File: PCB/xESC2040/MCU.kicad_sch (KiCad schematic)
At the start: 20 parts, among them J6 Conn_01x02, U2 RP2040, U3 W25Q128JVP, Y1 Crystal

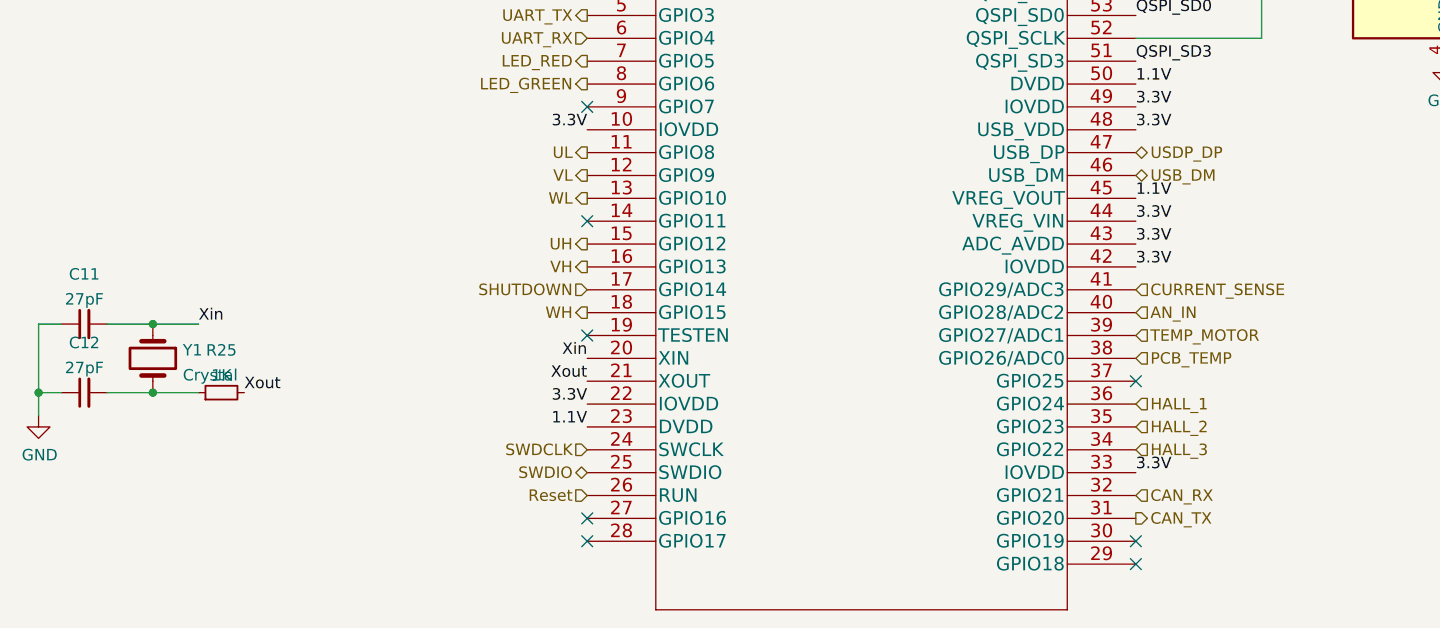
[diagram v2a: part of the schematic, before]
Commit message: added CAN, WIP
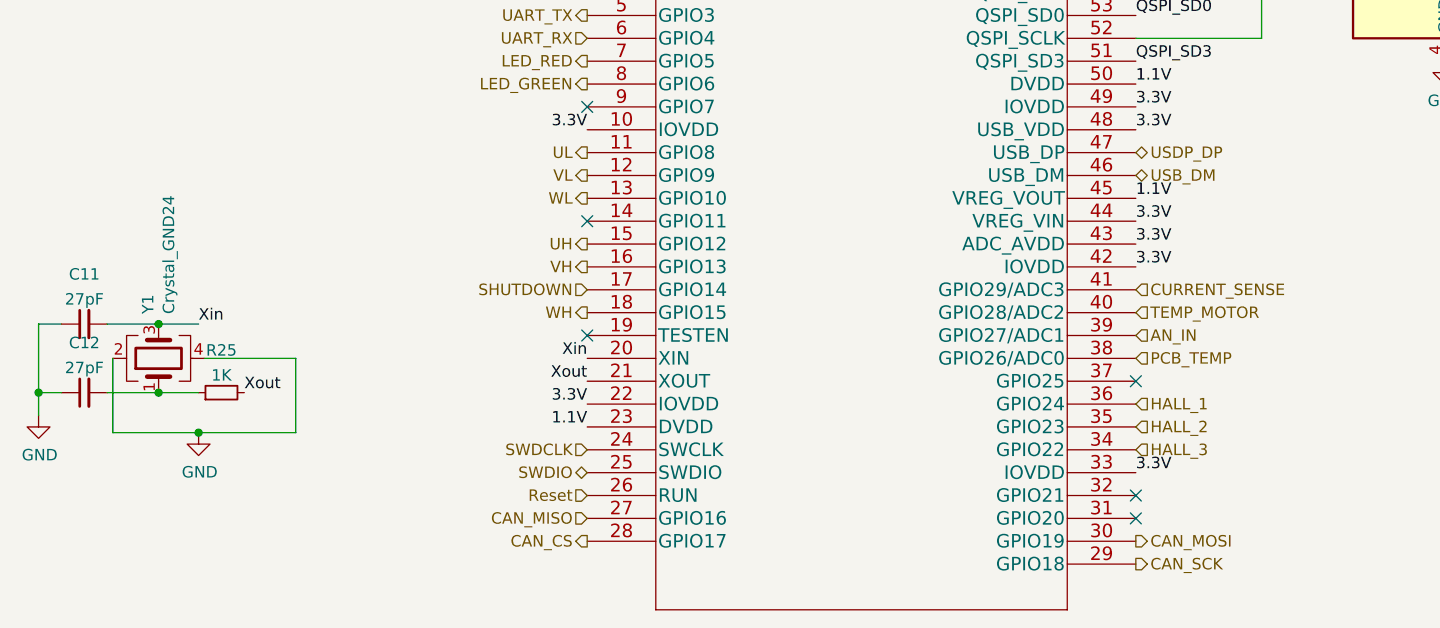
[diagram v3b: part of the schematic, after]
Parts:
- removed Y1: Crystal, Crystal:Crystal_SMD_3225-4Pin_3.2x2.5mm, symbol Device:Crystal
- added Y1: Crystal_GND24, Crystal:Crystal_SMD_3225-4Pin_3.2x2.5mm, symbol Device:Crystal_GND24
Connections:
- net AN_IN: now also U2.39 (GPIO27/ADC1); no longer U2.40 (GPIO28/ADC2)
- net GND: now also Y1.2, Y1.4
- net TEMP_MOTOR: now also U2.40 (GPIO28/ADC2); no longer U2.39 (GPIO27/ADC1)
- net Xin: now also Y1.3
- net CAN_MISO: now reaches U2.27 (GPIO16)
- net CAN_CS: now reaches U2.28 (GPIO17)
- net CAN_SCK: now reaches U2.29 (GPIO18)
- net CAN_MOSI: now reaches U2.30 (GPIO19)
- net at C12.2, R25.1: now also Y1.1
- net CAN_RX: no longer names the net of U2.32 (GPIO21)
- net CAN_TX: no longer names the net of U2.31 (GPIO20)
- no-connect marks 11 -> 9
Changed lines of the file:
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@@
   (junction (at 232.41 24.13) (diameter 0) (color 0 0 0 0)
   )
-  (junction (at 62.23 111.76) (diameter 0) (color 0 0 0 0)
+  (junction (at 67.31 123.825) (diameter 0) (color 0 0 0 0)
   )
   (junction (at 185.42 39.37) (diameter 0) (color 0 0 0 0)
@@
   (junction (at 177.8 21.59) (diameter 0) (color 0 0 0 0)
   )
+  (junction (at 62.865 111.76) (diameter 0) (color 0 0 0 0)
+  )
+  (junction (at 62.865 119.38) (diameter 0) (color 0 0 0 0)
+  )
   (junction (at 181.61 21.59) (diameter 0) (color 0 0 0 0)
   )
@@
   (junction (at 153.67 39.37) (diameter 0) (color 0 0 0 0)
   )
-  (junction (at 62.23 119.38) (diameter 0) (color 0 0 0 0)
-  )
   (junction (at 185.42 57.15) (diameter 0) (color 0 0 0 0)
   )
@@
   )
   (no_connect (at 110.49 100.33))
-  (no_connect (at 110.49 133.35))
   (no_connect (at 171.45 118.11))
   (no_connect (at 110.49 72.39))
   (no_connect (at 110.49 74.93))
+  (no_connect (at 171.45 130.81))
   (no_connect (at 110.49 69.85))
   (no_connect (at 110.49 87.63))
   (no_connect (at 110.49 113.03))
-  (no_connect (at 171.45 138.43))
-  (no_connect (at 171.45 135.89))
-  (no_connect (at 110.49 135.89))
+  (no_connect (at 171.45 133.35))
   (wire (pts (xy 185.42 74.93) (xy 185.42 80.01))
     (stroke (width 0) (type default) (color 0 0 0 0))
@@
     (stroke (width 0) (type default) (color 0 0 0 0))
   )
-  (wire (pts (xy 57.15 111.76) (xy 62.23 111.76))
+  (wire (pts (xy 57.15 111.76) (xy 62.865 111.76))
     (stroke (width 0) (type default) (color 0 0 0 0))
   )
@@
     (stroke (width 0) (type default) (color 0 0 0 0))
   )
+  (wire (pts (xy 62.865 119.38) (xy 67.31 119.38))
+    (stroke (width 0) (type default) (color 0 0 0 0))
+  )
   (wire (pts (xy 170.18 25.4) (xy 170.18 21.59))
     (stroke (width 0) (type default) (color 0 0 0 0))
@@
     (stroke (width 0) (type default) (color 0 0 0 0))
   )
+  (wire (pts (xy 67.945 115.57) (xy 78.105 115.57))
+    (stroke (width 0) (type default) (color 0 0 0 0))
+  )
   (wire (pts (xy 185.42 33.02) (xy 185.42 39.37))
     (stroke (width 0) (type default) (color 0 0 0 0))
@@
     (stroke (width 0) (type default) (color 0 0 0 0))
   )
+  (wire (pts (xy 78.105 115.57) (xy 78.105 123.825))
+    (stroke (width 0) (type default) (color 0 0 0 0))
+  )
   (wire (pts (xy 161.29 25.4) (xy 161.29 21.59))
     (stroke (width 0) (type default) (color 0 0 0 0))
   )
+  (wire (pts (xy 62.865 111.76) (xy 67.31 111.76))
+    (stroke (width 0) (type default) (color 0 0 0 0))
+  )
   (wire (pts (xy 146.05 21.59) (xy 153.67 21.59))
     (stroke (width 0) (type default) (color 0 0 0 0))
@@
     (stroke (width 0) (type default) (color 0 0 0 0))
   )
-  (wire (pts (xy 62.23 119.38) (xy 67.31 119.38))
+  (wire (pts (xy 78.105 123.825) (xy 67.31 123.825))
     (stroke (width 0) (type default) (color 0 0 0 0))
   )
@@
     (stroke (width 0) (type default) (color 0 0 0 0))
   )
-  (wire (pts (xy 62.23 111.76) (xy 67.31 111.76))
-    (stroke (width 0) (type default) (color 0 0 0 0))
-  )
   (wire (pts (xy 170.18 21.59) (xy 177.8 21.59))
     (stroke (width 0) (type default) (color 0 0 0 0))
@@
     (stroke (width 0) (type default) (color 0 0 0 0))
   )
-  (wire (pts (xy 57.15 119.38) (xy 62.23 119.38))
+  (wire (pts (xy 57.785 115.57) (xy 57.785 123.825))
+    (stroke (width 0) (type default) (color 0 0 0 0))
+  )
+  (wire (pts (xy 57.15 119.38) (xy 62.865 119.38))
     (stroke (width 0) (type default) (color 0 0 0 0))
   )
@@
   )
   (wire (pts (xy 52.07 111.76) (xy 49.53 111.76))
+    (stroke (width 0) (type default) (color 0 0 0 0))
+  )
+  (wire (pts (xy 67.31 123.825) (xy 57.785 123.825))
     (stroke (width 0) (type default) (color 0 0 0 0))
   )
@@
     (effects (font (size 1.27 1.27)) (justify left bottom))
   )
-  (hierarchical_label "CAN_TX" (shape output) (at 171.45 133.35 0)
-    (effects (font (size 1.27 1.27)) (justify left))
-  )
   (hierarchical_label "USDP_DP" (shape bidirectional) (at 171.45 92.71 0)
     (effects (font (size 1.27 1.27)) (justify left))
   )
+  (hierarchical_label "CAN_CS" (shape output) (at 110.49 135.89 180)
+    (effects (font (size 1.27 1.27)) (justify right))
+  )
   (hierarchical_label "UART_RX" (shape input) (at 110.49 80.01 180)
     (effects (font (size 1.27 1.27)) (justify right))
   )
-  (hierarchical_label "CAN_RX" (shape input) (at 171.45 130.81 0)
-    (effects (font (size 1.27 1.27)) (justify left))
-  )
-  (hierarchical_label "TEMP_MOTOR" (shape input) (at 171.45 113.03 0)
+  (hierarchical_label "TEMP_MOTOR" (shape input) (at 171.45 110.49 0)
     (effects (font (size 1.27 1.27)) (justify left))
   )
@@
     (effects (font (size 1.27 1.27)) (justify right))
   )
+  (hierarchical_label "CAN_MISO" (shape input) (at 110.49 133.35 180)
+    (effects (font (size 1.27 1.27)) (justify right))
+  )
   (hierarchical_label "Reset" (shape input) (at 110.49 130.81 180)
     (effects (font (size 1.27 1.27)) (justify right))
@@
     (effects (font (size 1.27 1.27)) (justify right))
   )
-  (hierarchical_label "AN_IN" (shape input) (at 171.45 110.49 0)
+  (hierarchical_label "AN_IN" (shape input) (at 171.45 113.03 0)
     (effects (font (size 1.27 1.27)) (justify left))
   )
@@
     (effects (font (size 1.27 1.27)) (justify right))
   )
+  (hierarchical_label "CAN_SCK" (shape output) (at 171.45 138.43 0)
+    (effects (font (size 1.27 1.27)) (justify left))
+  )
   (hierarchical_label "SWDIO" (shape bidirectional) (at 110.49 128.27 180)
     (effects (font (size 1.27 1.27)) (justify right))
@@
   )
   (hierarchical_label "HALL_2" (shape input) (at 171.45 123.19 0)
+    (effects (font (size 1.27 1.27)) (justify left))
+  )
+  (hierarchical_label "CAN_MOSI" (shape output) (at 171.45 135.89 0)
     (effects (font (size 1.27 1.27)) (justify left))
   )
@@
     (pin "8")
   )
-  (symbol (lib_id "Device:Crystal") (at 62.23 115.57 270) (unit 1)
-    (in_bom yes) (on_board yes) (fields_autoplaced)
-    (property "Reference" "Y1" (id 0) (at 65.5574 114.6615 90)
-      (effects (font (size 1.27 1.27)) (justify left))
-    )
-    (property "Value" "Crystal" (id 1) (at 65.5574 117.4366 90)
-      (effects (font (size 1.27 1.27)) (justify left))
-    )
-    (property "Footprint" "Crystal:Crystal_SMD_3225-4Pin_3.2x2.5mm" (id 2) (at 62.23 115.57 0)
-      (effects (font (size 1.27 1.27)) hide)
-    )
-    (property "Datasheet" "~" (id 3) (at 62.23 115.57 0)
-      (effects (font (size 1.27 1.27)) hide)
-    )
-    (property "Part Number" "" (id 4) (at 62.23 115.57 0)
-      (effects (font (size 1.27 1.27)) hide)
-    )
-    (pin "1")
-    (pin "2")
-  )
   (symbol (lib_id "Device:C") (at 146.05 29.21 0) (unit 1)
     (in_bom yes) (on_board yes)
@@
     (pin "1")
     (pin "2")
+  )
+  (symbol (lib_id "power:GND") (at 67.31 123.825 0) (unit 1)
+    (in_bom yes) (on_board yes)
+    (property "Reference" "#PWR0112" (id 0) (at 67.31 130.175 0)
+      (effects (font (size 1.27 1.27)) hide)
+    )
+    (property "Value" "GND" (id 1) (at 67.437 128.2192 0))
+    (property "Footprint" "" (id 2) (at 67.31 123.825 0)
+      (effects (font (size 1.27 1.27)) hide)
+    )
+    (property "Datasheet" "" (id 3) (at 67.31 123.825 0)
+      (effects (font (size 1.27 1.27)) hide)
+    )
+    (pin "1")
   )
   (symbol (lib_id "power:+3.3V") (at 205.74 55.88 0) (unit 1)
@@
     (pin "2")
   )
+  (symbol (lib_id "Device:Crystal_GND24") (at 62.865 115.57 90) (unit 1)
+    (in_bom yes) (on_board yes)
+    (property "Reference" "Y1" (id 0) (at 61.6966 110.6424 0)
+      (effects (font (size 1.27 1.27)) (justify left))
+    )
+    (property "Value" "Crystal_GND24" (id 1) (at 64.008 110.6424 0)
+      (effects (font (size 1.27 1.27)) (justify left))
+    )
+    (property "Footprint" "Crystal:Crystal_SMD_3225-4Pin_3.2x2.5mm" (id 2) (at 62.865 115.57 0)
+      (effects (font (size 1.27 1.27)) hide)
+    )
+    (property "Datasheet" "~" (id 3) (at 62.865 115.57 0)
+      (effects (font (size 1.27 1.27)) hide)
+    )
+    (property "Digikey" "50-ECS-80-12-33-JGN-CT-ND" (id 4) (at 62.865 115.57 0)
+      (effects (font (size 1.27 1.27)) hide)
+    )
+    (property "Part Number" "ECS-80-12-33-JGN-TR" (id 5) (at 62.865 115.57 0)
+      (effects (font (size 1.27 1.27)) hide)
+    )
+    (property "Stock_PN" "Y-4-SMD-8MhHz" (id 6) (at 62.865 115.57 0)
+      (effects (font (size 1.27 1.27)) hide)
+    )
+    (pin "1")
+    (pin "2")
+    (pin "3")
+    (pin "4")
+  )
   (symbol (lib_id "power:GND") (at 179.07 59.69 0) (unit 1)

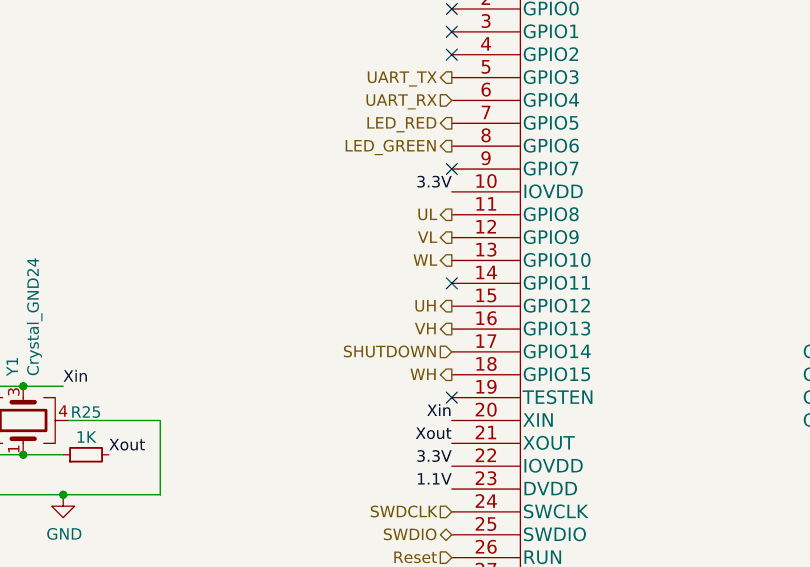
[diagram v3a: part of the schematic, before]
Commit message: added interrupt pin, added vias to the shunt, moved some stuff
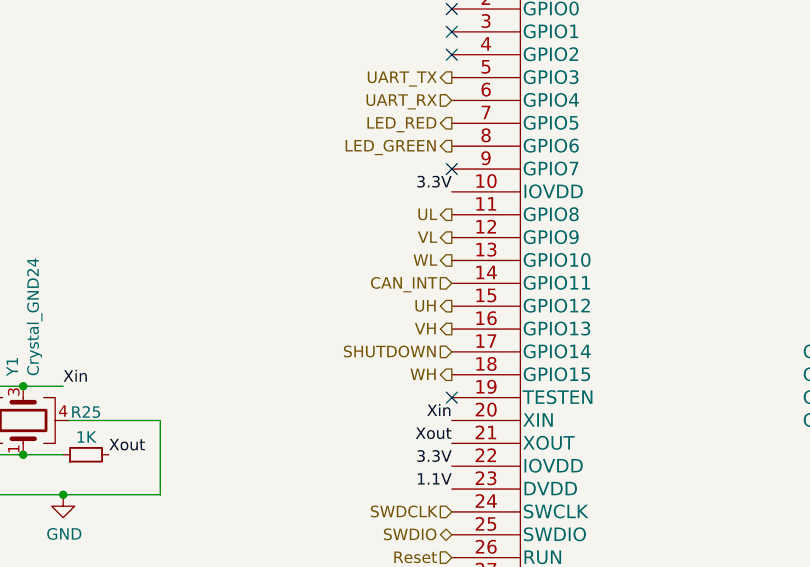
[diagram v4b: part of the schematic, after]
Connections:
- net CAN_INT: now reaches U2.14 (GPIO11)
- no-connect marks 9 -> 8
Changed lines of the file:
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@@
   (junction (at 177.8 39.37) (diameter 0) (color 0 0 0 0)
   )
-  (no_connect (at 110.49 100.33))
   (no_connect (at 171.45 118.11))
   (no_connect (at 110.49 72.39))
@@
     (effects (font (size 1.27 1.27)) (justify right))
   )
+  (hierarchical_label "CAN_INT" (shape input) (at 110.49 100.33 180)
+    (effects (font (size 1.27 1.27)) (justify right))
+  )

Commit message: Added some part numbers and such for the BoM.
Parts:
- C11, C12: Digikey (none) -> 311-1063-1-ND; Part Number (none) -> CC0603JRNPO9BN270; Stock_PN (none) -> C-603-27pF-50V-COG
- C13, C24: Digikey (none) -> 490-13409-1-ND; Part Number (none) -> CL10B105KA8NNNC; Stock_PN (none) -> C-603-1uF-25V-X7R
- R25, R26: Digikey (none) -> 311-1.00KHRDKR-ND; Part Number (none) -> RC0603FR-071KL; Stock_PN (none) -> R-603-1K-.1W-1%
- U2: Digikey (none) -> 2648-SC0914(13)CT-ND; Part Number (none) -> SC0914(13); Stock_PN (none) -> U-RP2040
- U3: Digikey (none) -> W25Q128JVPIMCT-ND; Part Number (none) -> W25Q128JVPIM; Stock_PN (none) -> U-W25Q128JVPIM
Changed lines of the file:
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@@
       (effects (font (size 1.524 1.524)))
+    )
+    (property "Digikey" "2648-SC0914(13)CT-ND" (id 4) (at 110.49 67.31 0)
+      (effects (font (size 1.27 1.27)) hide)
+    )
+    (property "Part Number" "SC0914(13)" (id 5) (at 110.49 67.31 0)
+      (effects (font (size 1.27 1.27)) hide)
+    )
+    (property "Stock_PN" "U-RP2040" (id 6) (at 110.49 67.31 0)
+      (effects (font (size 1.27 1.27)) hide)
     )
     (pin "1")
@@
       (effects (font (size 1.27 1.27)) hide)
     )
+    (property "Digikey" "W25Q128JVPIMCT-ND" (id 4) (at 205.74 72.39 0)
+      (effects (font (size 1.27 1.27)) hide)
+    )
+    (property "Part Number" "W25Q128JVPIM" (id 5) (at 205.74 72.39 0)
+      (effects (font (size 1.27 1.27)) hide)
+    )
+    (property "Stock_PN" "U-W25Q128JVPIM" (id 6) (at 205.74 72.39 0)
+      (effects (font (size 1.27 1.27)) hide)
+    )
     (pin "1")
     (pin "2")
@@
       (effects (font (size 1.27 1.27)) hide)
     )
+    (property "Digikey" "311-1063-1-ND" (id 4) (at 54.61 111.76 0)
+      (effects (font (size 1.27 1.27)) hide)
+    )
+    (property "Part Number" "CC0603JRNPO9BN270" (id 5) (at 54.61 111.76 0)
+      (effects (font (size 1.27 1.27)) hide)
+    )
+    (property "Stock_PN" "C-603-27pF-50V-COG" (id 6) (at 54.61 111.76 0)
+      (effects (font (size 1.27 1.27)) hide)
+    )
     (pin "1")
     (pin "2")
@@
     )
     (property "Datasheet" "~" (id 3) (at 241.3 27.94 0)
+      (effects (font (size 1.27 1.27)) hide)
+    )
+    (property "Digikey" "490-13409-1-ND" (id 4) (at 241.3 27.94 0)
+      (effects (font (size 1.27 1.27)) hide)
+    )
+    (property "Part Number" "CL10B105KA8NNNC" (id 5) (at 241.3 27.94 0)
+      (effects (font (size 1.27 1.27)) hide)
+    )
+    (property "Stock_PN" "C-603-1uF-25V-X7R" (id 6) (at 241.3 27.94 0)
       (effects (font (size 1.27 1.27)) hide)
     )
@@
       (effects (font (size 1.27 1.27)) hide)
     )
+    (property "Digikey" "311-1.00KHRDKR-ND" (id 4) (at 181.61 57.15 0)
+      (effects (font (size 1.27 1.27)) hide)
+    )
+    (property "Part Number" "RC0603FR-071KL" (id 5) (at 181.61 57.15 0)
+      (effects (font (size 1.27 1.27)) hide)
+    )
+    (property "Stock_PN" "R-603-1K-.1W-1%" (id 6) (at 181.61 57.15 0)
+      (effects (font (size 1.27 1.27)) hide)
+    )
     (pin "1")
     (pin "2")
@@
     )
     (property "Datasheet" "~" (id 3) (at 137.16 29.21 0)
+      (effects (font (size 1.27 1.27)) hide)
+    )
+    (property "Digikey" "490-13409-1-ND" (id 4) (at 137.16 29.21 0)
+      (effects (font (size 1.27 1.27)) hide)
+    )
+    (property "Part Number" "CL10B105KA8NNNC" (id 5) (at 137.16 29.21 0)
+      (effects (font (size 1.27 1.27)) hide)
+    )
+    (property "Stock_PN" "C-603-1uF-25V-X7R" (id 6) (at 137.16 29.21 0)
       (effects (font (size 1.27 1.27)) hide)
     )
@@
       (effects (font (size 1.27 1.27)) hide)
     )
+    (property "Digikey" "311-1.00KHRDKR-ND" (id 4) (at 69.85 119.38 0)
+      (effects (font (size 1.27 1.27)) hide)
+    )
+    (property "Part Number" "RC0603FR-071KL" (id 5) (at 69.85 119.38 0)
+      (effects (font (size 1.27 1.27)) hide)
+    )
+    (property "Stock_PN" "R-603-1K-.1W-1%" (id 6) (at 69.85 119.38 0)
+      (effects (font (size 1.27 1.27)) hide)
+    )
     (pin "1")
     (pin "2")
@@
       (effects (font (size 1.27 1.27)) hide)
     )
+    (property "Digikey" "311-1063-1-ND" (id 4) (at 54.61 119.38 0)
+      (effects (font (size 1.27 1.27)) hide)
+    )
+    (property "Part Number" "CC0603JRNPO9BN270" (id 5) (at 54.61 119.38 0)
+      (effects (font (size 1.27 1.27)) hide)
+    )
+    (property "Stock_PN" "C-603-27pF-50V-COG" (id 6) (at 54.61 119.38 0)
+      (effects (font (size 1.27 1.27)) hide)
+    )

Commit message: add pn's for header pins - all cheapies from LSCS
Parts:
- J6: LCSC (none) -> C2935908; Part Number (none) -> DZ254R-11-02-63; Stock_PN (none) -> J-TH-1x2-.1
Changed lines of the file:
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@@
+      (effects (font (size 1.27 1.27)) hide)
+    )
+    (property "LCSC" "C2935908" (id 4) (at 173.99 59.69 0)
+      (effects (font (size 1.27 1.27)) hide)
+    )
+    (property "Part Number" "DZ254R-11-02-63" (id 5) (at 173.99 59.69 0)
+      (effects (font (size 1.27 1.27)) hide)
+    )
+    (property "Stock_PN" "J-TH-1x2-.1" (id 6) (at 173.99 59.69 0)
       (effects (font (size 1.27 1.27)) hide)
     )
